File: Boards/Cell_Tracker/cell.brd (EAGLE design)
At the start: 47 x 40.6 mm, 32 parts, among them IC1 NCV78M05BDTRKG, T1 Si1013, U2 LMR16020

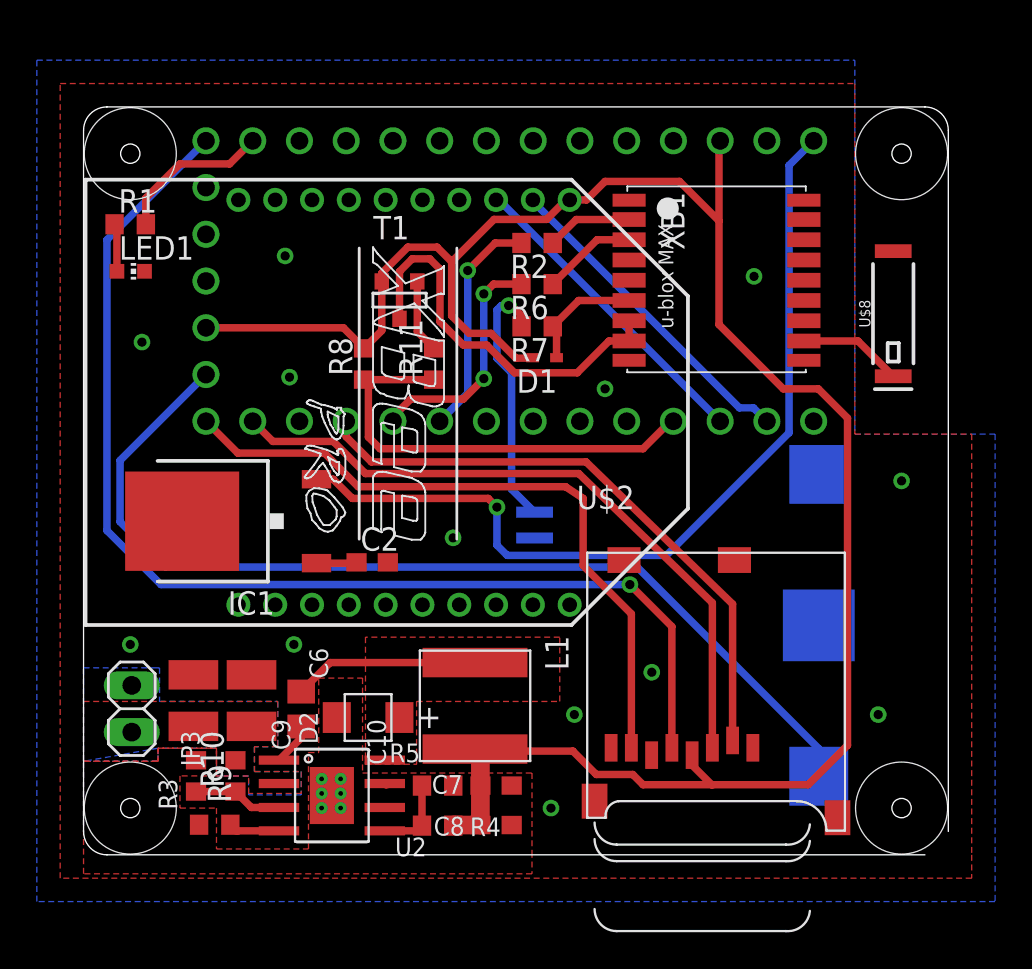
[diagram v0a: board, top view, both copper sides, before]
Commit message: Cell tracker V3 routed
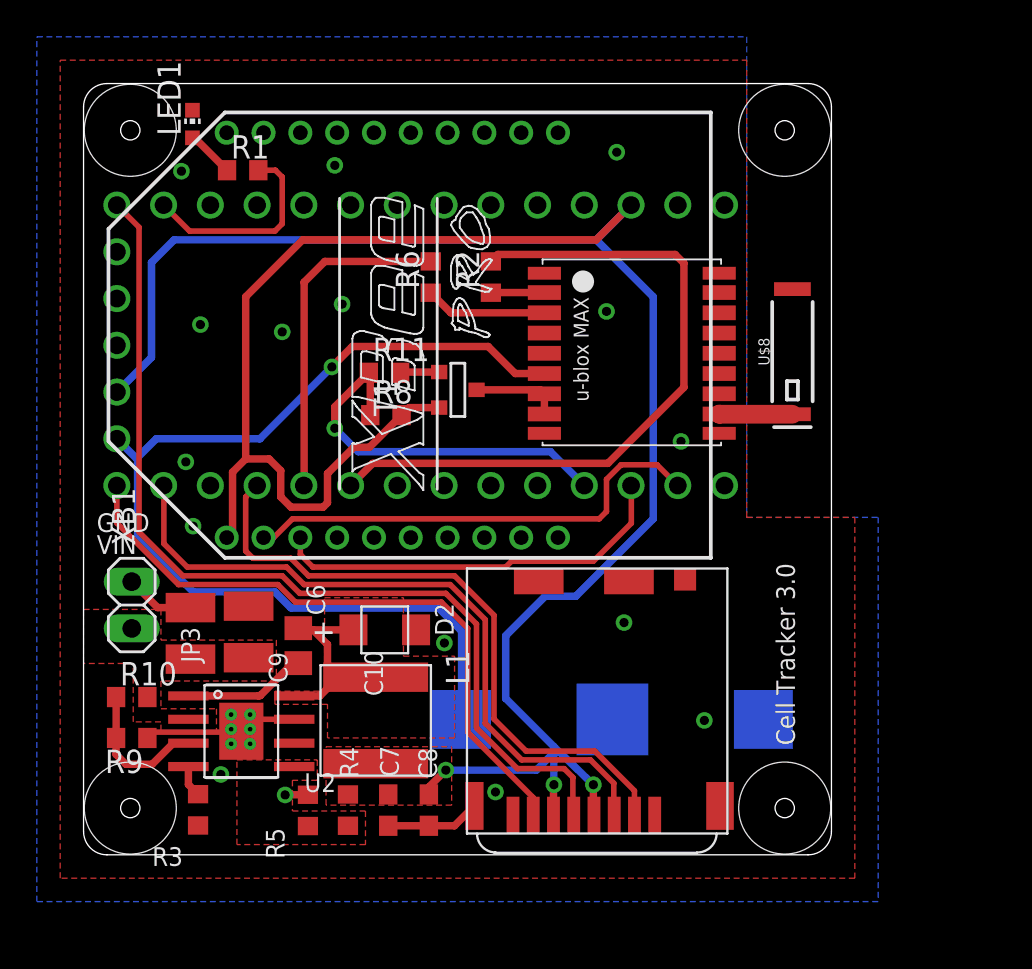
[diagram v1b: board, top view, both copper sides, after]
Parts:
- removed C1: (no value), jmolterLib:ELNASUPERCAP
- removed C2: 0.33uF, rcl:C0603
- removed D1: (no value), diode:SOD523
- removed IC1: NCV78M05BDTRKG, linear:DPACK_3
- removed R7: 22, rcl:R0603
- removed U$2: MICROSD, adafruit:MICROSD
- added U$3: MICRO_SD, NR_connectors:MICRO_SD_HINGED
- moved COIN 12.3 mm to (28.7, 7.36), turned to 180 degrees
- moved LED1 8.68 mm to (5.92, 39.7), turned to 0 degrees
- moved R5 7.18 mm to (12.2, 2.41), turned to 270 degrees
- moved R10 7.08 mm to (2.62, 8.57), turned to 0 degrees
- moved R1 6.78 mm to (8.65, 37.2)
- moved U$7 6.08 mm to (30.0, 27.2)
- moved U2 6.03 mm to (8.57, 6.72)
- moved C7 6.01 mm to (16.6, 2.43), turned to 270 degrees
- moved U$1 5.97 mm to (18.3, 27.7)
- moved U$8 5.85 mm to (38.5, 27.3)
- moved T1 5.85 mm to (20.3, 25.2), turned to 90 degrees
- moved R6 5.79 mm to (18.9, 31.4), turned to 90 degrees
- moved JP3 5.64 mm to (2.62, 13.6)
- moved L1 5.46 mm to (15.9, 7.30)
- moved R4 4.95 mm to (14.4, 2.43), turned to 90 degrees
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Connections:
- net N$14 renamed SW
- net N$15 renamed FB
- net N$16 renamed EN
- removed net +5V: IC1.3, U$1.VIN
- removed net N$12: COIN.+$1, U$1.VBAT
- removed net N$13: C1.3V3, R7.2
- net +3V3: now also U$3.VDD, U$3.VSS; no longer D1.A, U$2.4
- net GND: now also U$3.CD1, U$3.GND1, U$3.GND2, U$3.GND3, U$3.GND4; no longer C1.GND, C2.2, IC1.4, U$2.6, U$2.MT1, U$2.MT2
- net MISO: now also U$3.DAT0; no longer U$2.7
- net MOSI: now also U$3.CMD; no longer U$2.3
- net N$6: now also U$1.VIN; no longer C2.1, IC1.1
- net SCK: now also U$3.CLK; no longer U$2.5
- net SD_CS: now also U$3.CD; no longer U$2.2
- net V_BCKP: now also COIN.+$1, U$1.VBAT; no longer D1.C, R7.1
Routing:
- net N$12: track 54.5 -> 0.00 mm
- net V_BCKP: track 6.52 -> 55.6 mm, vias 0 -> 1
- net +5V: track 47.8 -> 0.00 mm, vias 1 -> 0
- net +3V3: track 110.0 -> 137.9 mm, vias 0 -> 3
- net RX3: track 12.4 -> 37.9 mm, vias 1 -> 0
- net GND: track 0.17 -> 17.4 mm, vias 19 -> 22
- net N$11: track 21.4 -> 4.87 mm
- net N$13: track 14.1 -> 0.00 mm, vias 1 -> 0
- net SCK: track 62.9 -> 52.7 mm, vias 1 -> 0
- net RX1: track 17.7 -> 25.6 mm
- net TX3: track 12.9 -> 18.4 mm, vias 2 -> 0
- net TX1: track 17.2 -> 22.2 mm
- net N$9: track 2.33 -> 7.09 mm
- net FB: track 4.31 -> 0.00 mm
- net GPSON: track 24.5 -> 21.0 mm, vias 0 -> 1
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- added copper zone on layer 1, net +3V3
- added copper zone on layer 1, net FB
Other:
- board size 47 x 40.6 mm -> 40.6 x 41.9 mm
- board text added: "Cell Tracker 3.0"
- board text added: "GND"
- board text added: "VIN"
